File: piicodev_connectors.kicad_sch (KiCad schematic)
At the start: 3 parts, among them J1501 Conn_01x04, J1502 Conn_01x04, U1501 D1213A-04TS-7

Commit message: Position final few components
Removed one ESD diode arrray - experimental board, so not really needed,
with the exception of the USB lines.

Add and position 5V indicator LED

Finished wiring up the 5V buck-boost regulator
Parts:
- J1502, U1501: now not fitted; now left out of the parts list
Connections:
- net +3V3: now also J1501.2 (Pin_2), J1502.2 (Pin_2)
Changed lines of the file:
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@@
+	)
+	(junction
+		(at 93.98 114.3)
+		(diameter 0)
+		(color 0 0 0 0)
 	)
 	(junction
@@
 	)
 	(junction
+		(at 76.2 101.6)
+		(diameter 0)
+		(color 0 0 0 0)
+	)
+	(junction
 		(at 81.28 111.76)
 		(diameter 0)
@@
 	(wire
 		(pts
+			(xy 76.2 101.6) (xy 93.98 101.6)
+		)
+		(stroke
+			(width 0)
+			(type default)
+		)
+	)
+	(wire
+		(pts
 			(xy 66.04 129.54) (xy 66.04 121.92)
 		)
@@
 		(pts
 			(xy 66.04 142.24) (xy 71.12 142.24)
+		)
+		(stroke
+			(width 0)
+			(type default)
+		)
+	)
+	(wire
+		(pts
+			(xy 93.98 101.6) (xy 93.98 114.3)
 		)
 		(stroke
@@
 		(at 76.2 132.08 0)
 		(unit 1)
-		(exclude_from_sim no)
-		(in_bom yes)
-		(on_board yes)
-		(dnp no)
+		(exclude_from_sim yes)
+		(in_bom no)
+		(on_board no)
+		(dnp yes)
 		(fields_autoplaced yes)
 		(property "Reference" "U1501"
@@
 		(mirror x)
 		(unit 1)
-		(exclude_from_sim no)
-		(in_bom yes)
-		(on_board yes)
-		(dnp no)
+		(exclude_from_sim yes)
+		(in_bom no)
+		(on_board no)
+		(dnp yes)
 		(fields_autoplaced yes)
 		(property "Reference" "J1502"

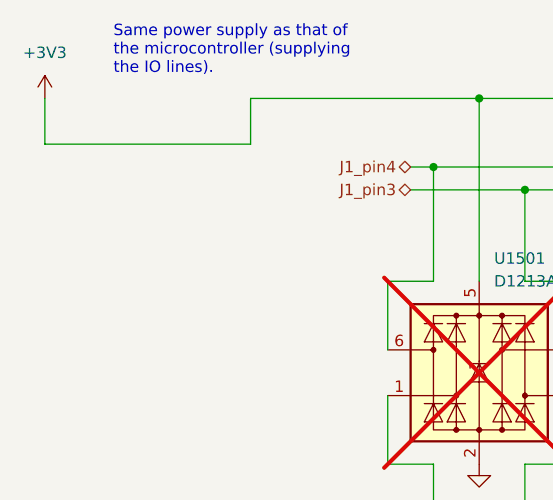
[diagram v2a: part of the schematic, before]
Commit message: Wire remaining traces, fix DRC errors
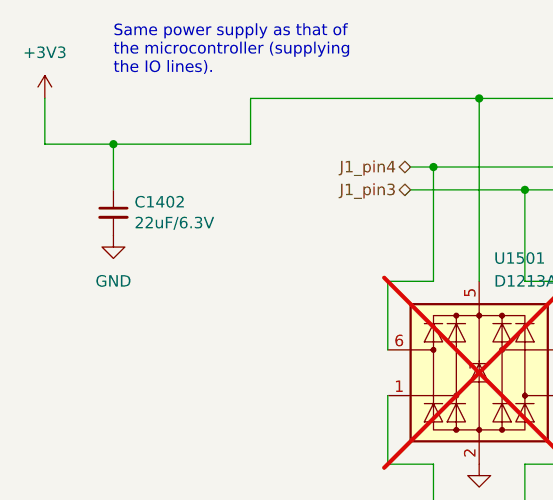
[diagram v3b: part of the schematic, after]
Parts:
- added C1402: 22uF/6.3V, Capacitor_SMD:C_0603_1608Metric, symbol Device:C_Small
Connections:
- net +3V3: now also C1402.1
- net GND: now also C1402.2
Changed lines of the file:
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@@
+	)
+	(junction
+		(at 35.56 106.68)
+		(diameter 0)
+		(color 0 0 0 0)
 	)
 	(junction
@@
 	(wire
 		(pts
+			(xy 35.56 106.68) (xy 35.56 111.76)
+		)
+		(stroke
+			(width 0)
+			(type default)
+		)
+	)
+	(wire
+		(pts
 			(xy 81.28 152.4) (xy 93.98 152.4)
 		)
@@
 	(wire
 		(pts
-			(xy 27.94 106.68) (xy 50.8 106.68)
+			(xy 27.94 106.68) (xy 35.56 106.68)
 		)
 		(stroke
@@
 		(pts
 			(xy 71.12 154.94) (xy 93.98 154.94)
+		)
+		(stroke
+			(width 0)
+			(type default)
+		)
+	)
+	(wire
+		(pts
+			(xy 35.56 106.68) (xy 50.8 106.68)
 		)
 		(stroke
@@
 	)
 	(symbol
+		(lib_id "Device:C_Small")
+		(at 35.56 114.3 0)
+		(unit 1)
+		(exclude_from_sim no)
+		(in_bom yes)
+		(on_board yes)
+		(dnp no)
+		(property "Reference" "C1402"
+			(at 37.8968 113.1316 0)
+			(effects
+				(font
+					(size 1.27 1.27)
+				)
+				(justify left)
+			)
+		)
+		(property "Value" "22uF/6.3V"
+			(at 37.8968 115.443 0)
+			(effects
+				(font
+					(size 1.27 1.27)
+				)
+				(justify left)
+			)
+		)
+		(property "Footprint" "Capacitor_SMD:C_0603_1608Metric"
+			(at 35.56 114.3 0)
+			(effects
+				(font
+					(size 1.27 1.27)
+				)
+				(hide yes)
+			)
+		)
+		(property "Datasheet" "~"
+			(at 35.56 114.3 0)
+			(effects
+				(font
+					(size 1.27 1.27)
+				)
+				(hide yes)
+			)
+		)
+		(property "Description" ""
+			(at 35.56 114.3 0)
+			(effects
+				(font
+					(size 1.27 1.27)
+				)
+				(hide yes)
+			)
+		)
+		(property "LCSC" "C59461"
+			(at 35.56 114.3 0)
+			(effects
+				(font
+					(size 1.27 1.27)
+				)
+				(hide yes)
+			)
+		)
+		(pin "1"
+		)
+		(pin "2"
+		)
+		(instances
+			(project "ESP_bare_chip_test_board"
+				(path "/45b6f84a-e69b-48be-a49b-bc68872e2c15/04b60eee-d553-4abe-8b22-3fc74b6351bd"
+					(reference "C1402")
+					(unit 1)
+				)
+			)
+		)
+	)
+	(symbol
 		(lib_id "Connector_Generic_MountingPin:Conn_01x04_MountingPin")
 		(at 99.06 157.48 0)
@@
 					(unit 1)
 				)
+			)
+		)
+	)
+	(symbol
+		(lib_id "power:GND")
+		(at 35.56 116.84 0)
+		(unit 1)
+		(exclude_from_sim no)
+		(in_bom yes)
+		(on_board yes)
+		(dnp no)
+		(fields_autoplaced yes)
+		(property "Reference" "#PWR01404"
+			(at 35.56 123.19 0)
+			(effects
+				(font
+					(size 1.27 1.27)
+				)
+				(hide yes)
+			)
+		)
+		(property "Value" "GND"
+			(at 35.56 121.92 0)
+			(effects
+				(font
+					(size 1.27 1.27)
+				)
+			)
+		)
+		(property "Footprint" ""
+			(at 35.56 116.84 0)
+			(effects
+				(font
+					(size 1.27 1.27)
+				)
+				(hide yes)
+			)
+		)
+		(property "Datasheet" ""
+			(at 35.56 116.84 0)
+			(effects
+				(font
+					(size 1.27 1.27)
+				)
+				(hide yes)
+			)
+		)
+		(property "Description" "Power symbol creates a global label with name \"GND\" , ground"
+			(at 35.56 116.84 0)
+			(effects
+				(font
+					(size 1.27 1.27)
+				)
+				(hide yes)
+			)
+		)
+		(pin "1"
+		)
+		(instances
+			(project "ESP_bare_chip_test_board"
+				(path "/45b6f84a-e69b-48be-a49b-bc68872e2c15/04b60eee-d553-4abe-8b22-3fc74b6351bd"
+					(reference "#PWR01404")
+					(unit 1)
+				)

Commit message: Silkscreen work. Edit tittle block/version number
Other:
- company: (c) -> (c) Vincent Dalstra
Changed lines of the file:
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@@
 	(title_block
 		(title "Untitled 4-layer JLCPCB")
-		(date "1984/04/01")
-		(rev "v1.0.0")
-		(company "(c)")
+		(date "2024-06-14")
+		(rev "1.0.0")
+		(company "(c) Vincent Dalstra")
 	)
 	(junction
